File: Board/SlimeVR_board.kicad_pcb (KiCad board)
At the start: 2 copper layers, 61 x 50 mm, 45 parts, among them IC1 HT7833, J1 USB_C_Receptacle_USB2.0_16P, J2 JST-PH, J3 SMD_Pads, J4 SMD_Pads, J5 Conn_01x01_Pin, J6 Conn_01x01_Pin, J7 JTX-HX-A-1, J8 JTX-HX-A-1, Q1 DMP3099L-7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

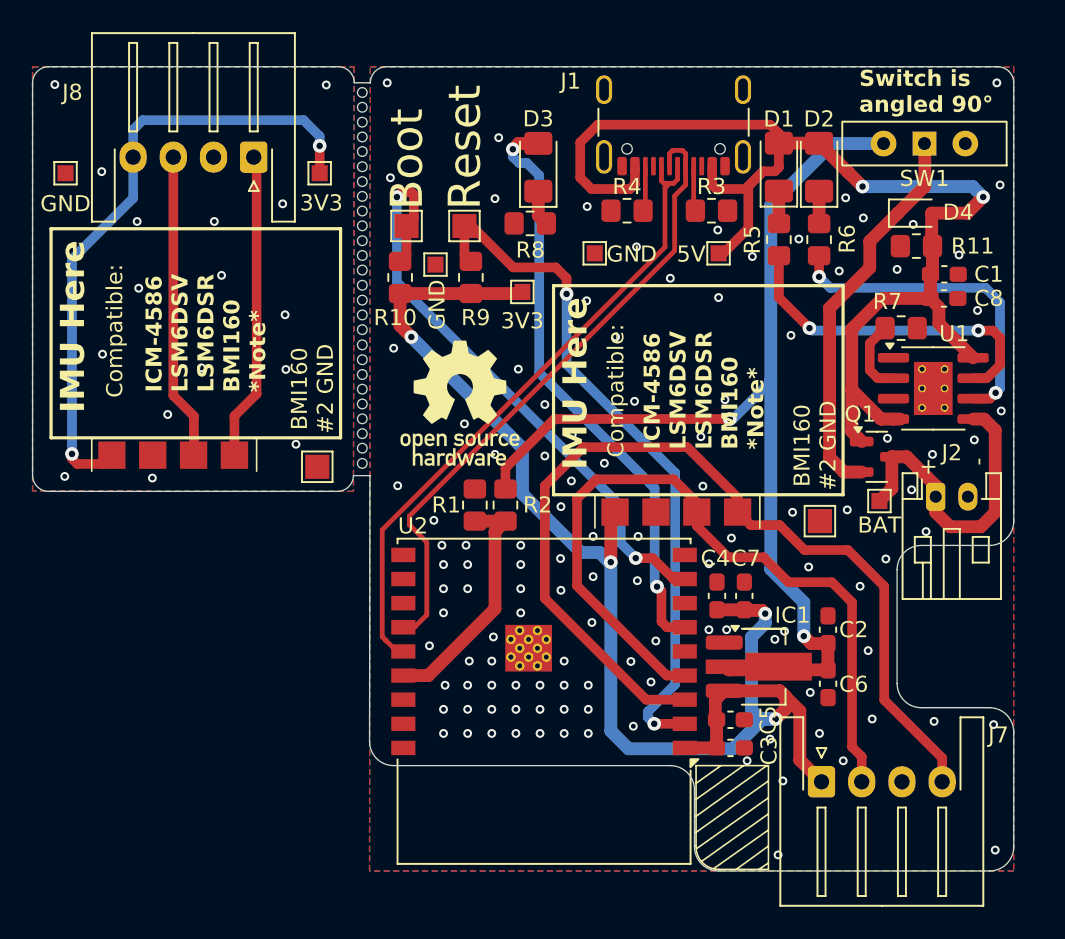
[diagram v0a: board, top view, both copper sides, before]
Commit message: Redisign, Power Supply improved
Removed reset pin becuse just hardware off > on
Added physical button for boot
HT7833 replaced for XC6220B331MR becuse HT7833 not working :(
Small design silkscreen changes
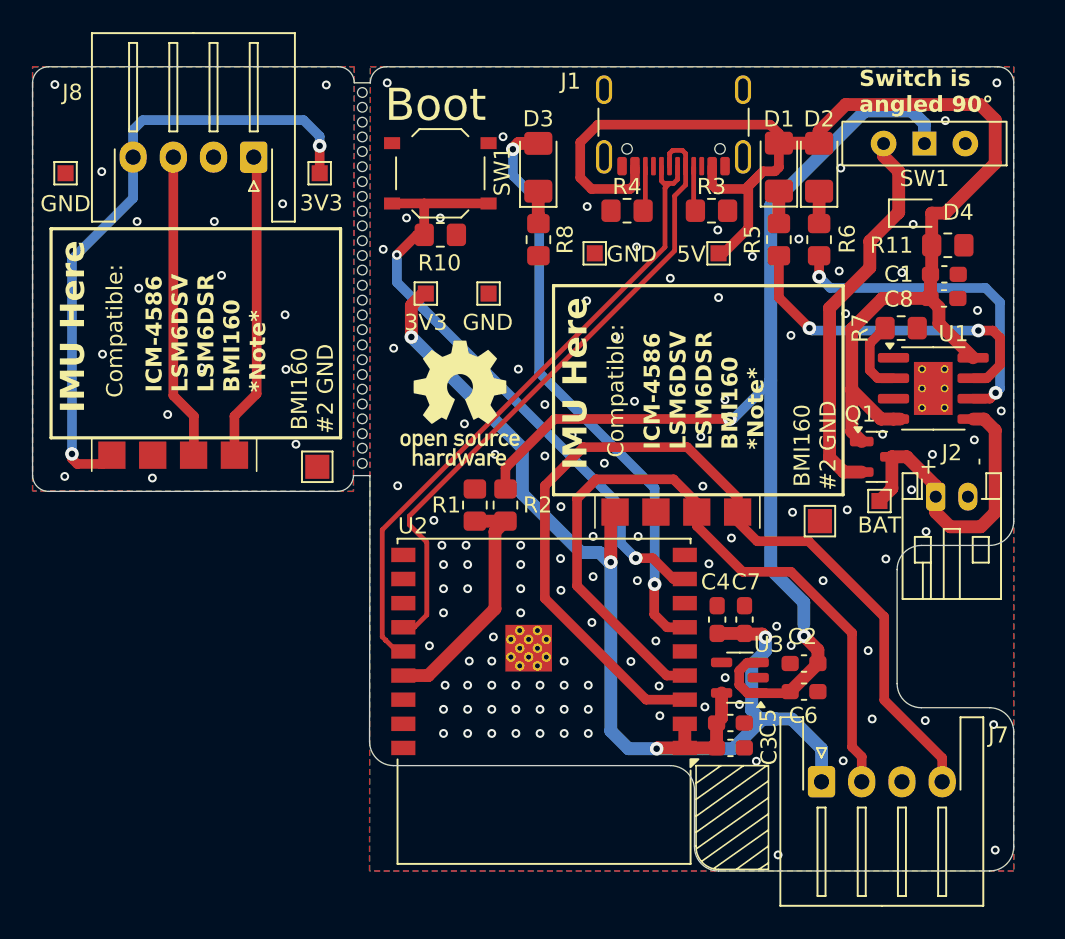
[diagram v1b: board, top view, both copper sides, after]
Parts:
- removed IC1: HT7833, Package_TO_SOT_SMD:SOT-89-3_Handsoldering
- removed J5, J6: Conn_01x01_Pin, TestPoint:TestPoint_Pad_1.5x1.5mm
- removed R9: 10k, Resistor_SMD:R_0805_2012Metric_Pad1.20x1.40mm_HandSolder
- added SW2: SW_Push, Button_Switch_SMD:SW_Push_1P1T_XKB_TS-1187A, F.Cu at (60.9, 26.3)
- added U3: XC6220B331MR, Package_TO_SOT_SMD:SOT-23-5, F.Cu at (79.5, 57.7)
- C3: value 47uF -> 10uF
- D4: value 1N4448WSF-7 -> 1N4007WS
- moved 3V3 6.00 mm to (60.0, 33.8)
- moved GND 3.76 mm to (63.9, 33.8)
- moved R10 3.64 mm to (60.9, 30.1), turned to 180 degrees
- moved C2 2.57 mm to (83.5, 56.8), turned to 180 degrees
- moved R11 1.95 mm to (92.5, 30.8), turned to 180 degrees
- moved C6 1.57 mm to (83.5, 58.5), turned to 0 degrees
- moved C4 1.47 mm to (78.1, 54.1)
- moved C7 1.47 mm to (79.8, 54.1)
- moved R8 1.13 mm to (67.0, 30.4), turned to 90 degrees
- moved C5 0.20 mm to (78.9, 60.5)
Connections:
- C2 pad 1: Net-(SW1-C) -> Net-(SW1-B)
- C6 pad 1: Net-(SW1-C) -> Net-(SW1-B)
- R2 pad 1: Net-(SW1-C) -> Net-(SW1-B)
- SW1 pad 2: unconnected-(SW1-B-Pad2) -> Net-(SW1-B)
- SW1 pad 3: Net-(SW1-C) -> unconnected-(SW1-C-Pad3)
- U2 pad 2: Net-(J5-Pin_1) -> +3.3V
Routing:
- net Net-(SW1-B): track 0.00 -> 70.8 mm, vias 0 -> 2
- net Net-(SW1-C): track 66.1 -> 0.00 mm, vias 2 -> 0
- net Net-(J5-Pin_1): track 43.3 -> 0.00 mm, vias 2 -> 0
- net +3.3V: track 124.9 -> 112.3 mm
- net +5V: track 79.7 -> 85.5 mm, vias 2 -> 0
- net SCL: track 66.5 -> 65.4 mm
- net Net-(U2-IO9): track 37.9 -> 38.8 mm
- net SDA: track 77.3 -> 76.6 mm
- net Earth: vias 132 -> 127
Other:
- board text added: "SW1"
- board text removed: "Reset"

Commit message: Updated pcb
Fixed pull up rezistor not connected
Fixed small conection of 5V to LDO
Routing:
- net +3.3V: track 112.3 -> 116.8 mm
- net Net-(SW1-B): track 70.8 -> 71.5 mm
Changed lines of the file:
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@@
+	)
+	(segment
+		(start 61.9 31.9)
+		(end 61.9 30.15)
+		(width 0.8)
+		(layer "F.Cu")
+		(net 24)
 	)
 	(segment
@@
 		(start 78.3875 58.632602)
 		(end 78.3875 60.1875)
+		(width 0.8)
+		(layer "F.Cu")
+		(net 24)
+	)
+	(segment
+		(start 60 33.8)
+		(end 61.9 31.9)
 		(width 0.8)
 		(layer "F.Cu")
@@
 	)
 	(segment
+		(start 83.5 55.0875)
+		(end 83.5 53)
+		(width 0.8)
+		(layer "B.Cu")
+		(net 31)
+	)
+	(segment
+		(start 83.5125 55.1)
+		(end 83.5 55.0875)
+		(width 0.8)
+		(layer "B.Cu")
+		(net 31)
+	)
+	(segment
+		(start 81.444 28.306)
+		(end 87.3 22.45)
+		(width 0.8)
+		(layer "B.Cu")
+		(net 31)
+	)
+	(segment
 		(start 83.5 53)
 		(end 81.444 50.944)
@@
 	)
 	(segment
-		(start 81.444 28.306)
-		(end 87.3 22.45)
-		(width 0.8)
-		(layer "B.Cu")
-		(net 31)
-	)
-	(segment
 		(start 81.444 39.256)
 		(end 81.444 39.2)
@@
 	)
 	(segment
+		(start 81.444 50.944)
+		(end 81.444 39.2)
+		(width 0.8)
+		(layer "B.Cu")
+		(net 31)
+	)
+	(segment
 		(start 78.9 41.6)
 		(end 79.1 41.6)
@@
 	)
 	(segment
-		(start 81.444 50.944)
-		(end 81.444 39.2)
-		(width 0.8)
-		(layer "B.Cu")
-		(net 31)
-	)
-	(segment
 		(start 91 23.25)
 		(end 91 24.475)
@@
 		(layer "B.Cu")
 		(net 31)
-	)
-	(segment
-		(start 83.5 54.367398)
-		(end 83.5 53)
-		(width 0.8)
-		(layer "B.Cu")
-		(net 31)
